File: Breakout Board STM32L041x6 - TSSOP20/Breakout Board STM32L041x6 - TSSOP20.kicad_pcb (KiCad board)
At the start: 2 copper layers, 35.6 x 33 mm, 31 parts, among them J1 Conn_01x10, J2 Conn_01x10, SW1 reset switch, SW2 switch, U1 STM32L041F6P7, Y1 Crystal 32768

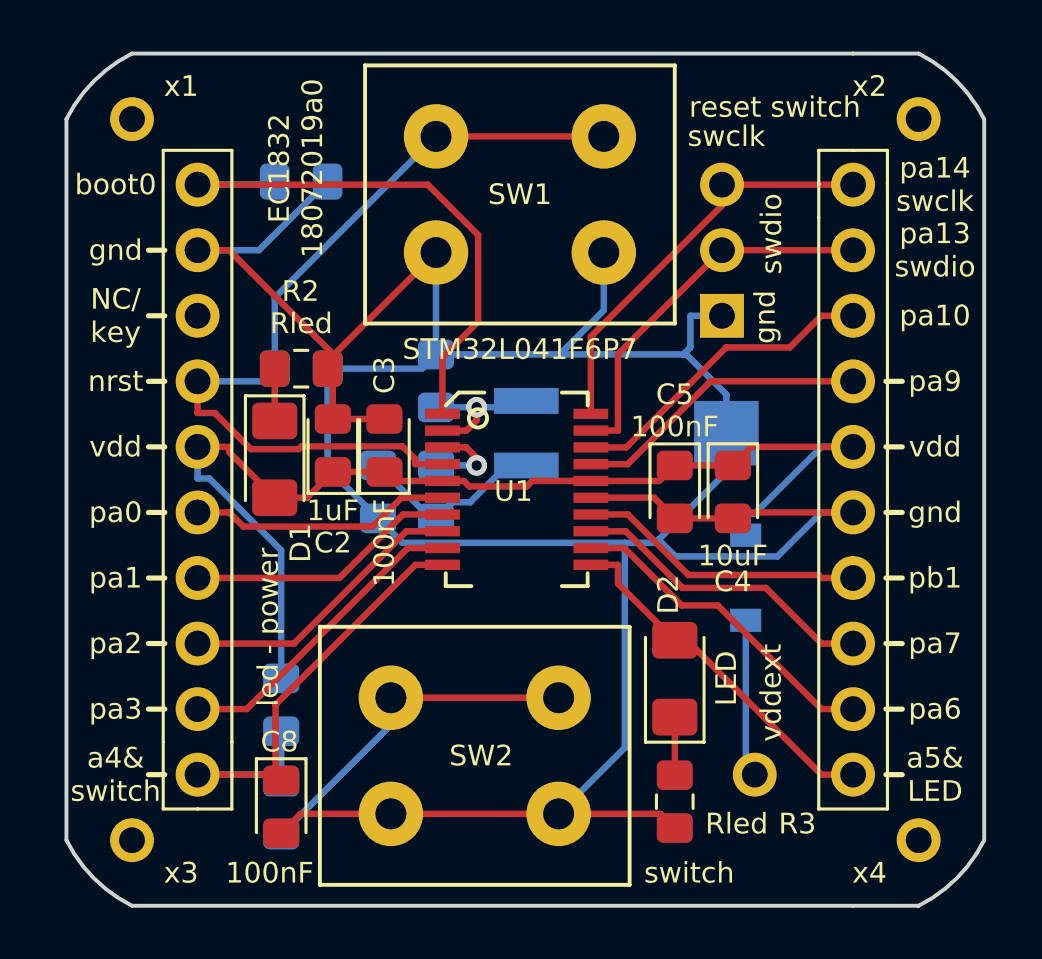
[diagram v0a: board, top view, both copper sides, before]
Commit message: Add ground vias and ground fill zones
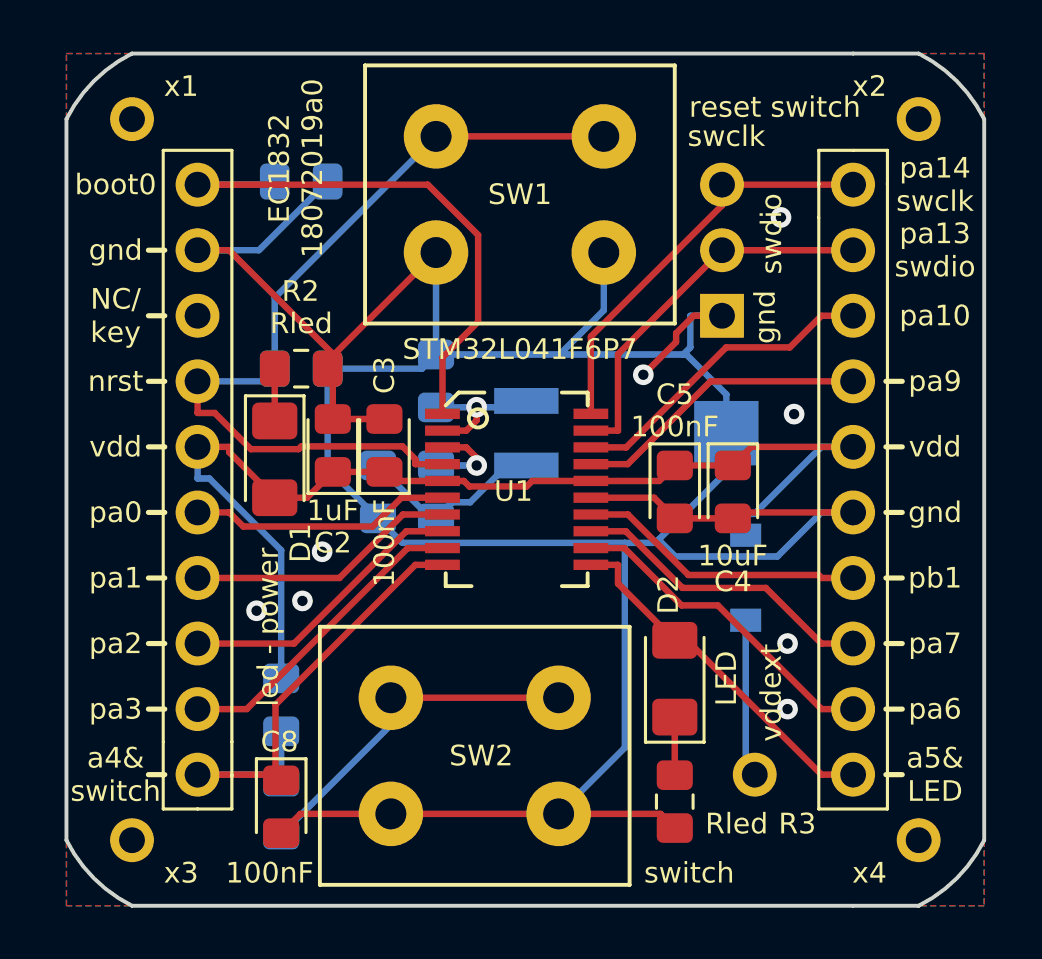
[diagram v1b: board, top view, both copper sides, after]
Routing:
- net GND: track 122.2 -> 126.4 mm, vias 0 -> 8
- added copper zone on B.Cu, net GND
- added copper zone on F.Cu, net GND
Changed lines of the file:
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@@
     (thickness 1.6)
     (drawings 97)
-    (tracks 181)
+    (tracks 193)
     (zones 0)
     (modules 31)
@@
   (segment (start 126.37 76.43) (end 124.42 74.48) (width 0.25) (layer B.Cu) (net 2))
   (segment (start 124.42 74.48) (end 124.42 70.63) (width 0.25) (layer B.Cu) (net 2))
+  (via (at 123.444 79.629) (size 0.8) (drill 0.4) (layers F.Cu B.Cu) (net 2))
+  (via (at 124.206 77.724) (size 0.8) (drill 0.4) (layers F.Cu B.Cu) (net 2))
+  (via (at 142.24 81.28) (size 0.8) (drill 0.4) (layers F.Cu B.Cu) (net 2))
+  (via (at 142.24 83.82) (size 0.8) (drill 0.4) (layers F.Cu B.Cu) (net 2))
+  (via (at 141.986 64.77) (size 0.8) (drill 0.4) (layers F.Cu B.Cu) (net 2))
+  (via (at 136.652 70.866) (size 0.8) (drill 0.4) (layers F.Cu B.Cu) (net 2))
+  (segment (start 138.6 68.58) (end 137.922 69.258) (width 0.25) (layer F.Cu) (net 2))
+  (segment (start 139.7 68.58) (end 138.6 68.58) (width 0.25) (layer F.Cu) (net 2))
+  (segment (start 137.922 69.596) (end 136.652 70.866) (width 0.25) (layer F.Cu) (net 2))
+  (segment (start 137.922 69.258) (end 137.922 69.596) (width 0.25) (layer F.Cu) (net 2))
+  (via (at 142.494 72.39) (size 0.8) (drill 0.4) (layers F.Cu B.Cu) (net 2))
+  (via (at 121.666 80.01) (size 0.8) (drill 0.4) (layers F.Cu B.Cu) (net 2))
   (segment (start 140.62 77.08) (end 140.62 76.2547) (width 0.25) (layer B.Cu) (net 3))
   (segment (start 144.78 73.66) (end 143.5547 73.66) (width 0.25) (layer B.Cu) (net 3))
@@
   (segment (start 143.5547 86.36) (end 138.3497 81.155) (width 0.25) (layer F.Cu) (net 24))
   (segment (start 138.3497 81.155) (end 137.87 81.155) (width 0.25) (layer F.Cu) (net 24))
+  (zone (net 2) (net_name GND) (layer F.Cu) (hatch edge 0.508)
+    (connect_pads (clearance 0.508))
+    (min_thickness 0.254)
+    (fill yes (arc_segments 16) (thermal_gap 0.508) (thermal_bridge_width 0.508))
+    (polygon
+      (pts
+        (xy 114.3 58.42) (xy 149.86 58.42) (xy 149.86 91.44) (xy 114.3 91.44)
+      )
+    )
+  )
+  (zone (net 2) (net_name GND) (layer B.Cu) (hatch edge 0.508)
+    (connect_pads (clearance 0.508))
+    (min_thickness 0.254)
+    (fill yes (arc_segments 16) (thermal_gap 0.508) (thermal_bridge_width 0.508))
+    (polygon
+      (pts
+        (xy 114.3 58.42) (xy 149.86 58.42) (xy 149.86 91.44) (xy 114.3 91.44)
+      )
+    )
+  )
 )
